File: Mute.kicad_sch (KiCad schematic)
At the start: 15 parts, among them Q1 AO3400A, SW7 SW_Push, U8 74LVC1G17, U9 SN74LVC2G74

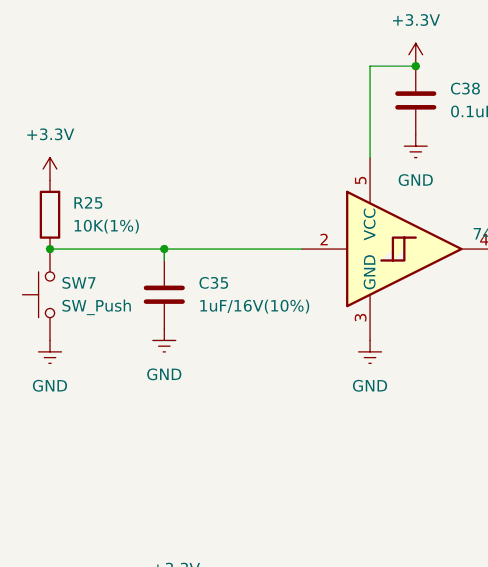
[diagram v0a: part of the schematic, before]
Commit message: Initial population of PCB
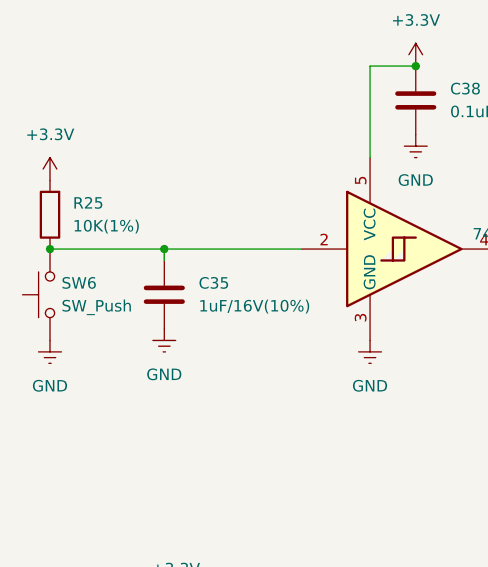
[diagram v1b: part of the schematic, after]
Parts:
- removed SW7: SW_Push, symbol Switch:SW_Push
- added SW6: SW_Push, Button_Switch_SMD:SW_SPST_PTS645, symbol Switch:SW_Push
- U8: footprint (none) -> Package_TO_SOT_SMD:SOT-23-5
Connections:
- net GND: now also SW6.1
- net at C35.1, R25.1, U8.2: now also SW6.2
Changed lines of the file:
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@@
-	)
-	(symbol
-		(lib_id "Switch:SW_Push")
-		(at 40.64 68.58 90)
-		(unit 1)
-		(exclude_from_sim no)
-		(in_bom yes)
-		(on_board yes)
-		(dnp no)
-		(fields_autoplaced yes)
-		(property "Reference" "SW7"
-			(at 41.91 67.3099 90)
-			(effects
-				(font
-					(size 1.27 1.27)
-				)
-				(justify right)
-			)
-		)
-		(property "Value" "SW_Push"
-			(at 41.91 69.8499 90)
-			(effects
-				(font
-					(size 1.27 1.27)
-				)
-				(justify right)
-			)
-		)
-		(property "Footprint" ""
-			(at 35.56 68.58 0)
-			(effects
-				(font
-					(size 1.27 1.27)
-				)
-				(hide yes)
-			)
-		)
-		(property "Datasheet" "~"
-			(at 35.56 68.58 0)
-			(effects
-				(font
-					(size 1.27 1.27)
-				)
-				(hide yes)
-			)
-		)
-		(property "Description" "Push button switch, generic, two pins"
-			(at 40.64 68.58 0)
-			(effects
-				(font
-					(size 1.27 1.27)
-				)
-				(hide yes)
-			)
-		)
-		(pin "2"
-		)
-		(pin "1"
-		)
-		(instances
-			(project "Wave"
-				(path "/d9ae5ab6-a812-4d0b-96e5-05f704754669/797be30f-7ee7-478f-9b58-a053d36acba1"
-					(reference "SW7")
-					(unit 1)
-				)
-			)
-		)
 	)
 	(symbol
@@
 			)
 		)
-		(property "Footprint" ""
+		(property "Footprint" "Package_TO_SOT_SMD:SOT-23-5"
 			(at 78.74 63.5 0)
 			(effects
@@
 					(unit 1)
 				)
+			)
+		)
+	)
+	(symbol
+		(lib_id "Switch:SW_Push")
+		(at 40.64 68.58 90)
+		(unit 1)
+		(exclude_from_sim no)
+		(in_bom yes)
+		(on_board yes)
+		(dnp no)
+		(fields_autoplaced yes)
+		(property "Reference" "SW6"
+			(at 41.91 67.3099 90)
+			(effects
+				(font
+					(size 1.27 1.27)
+				)
+				(justify right)
+			)
+		)
+		(property "Value" "SW_Push"
+			(at 41.91 69.8499 90)
+			(effects
+				(font
+					(size 1.27 1.27)
+				)
+				(justify right)
+			)
+		)
+		(property "Footprint" "Button_Switch_SMD:SW_SPST_PTS645"
+			(at 35.56 68.58 0)
+			(effects
+				(font
+					(size 1.27 1.27)
+				)
+				(hide yes)
+			)
+		)
+		(property "Datasheet" "~"
+			(at 35.56 68.58 0)
+			(effects
+				(font
+					(size 1.27 1.27)
+				)
+				(hide yes)
+			)
+		)
+		(property "Description" "Push button switch, generic, two pins"
+			(at 40.64 68.58 0)
+			(effects
+				(font
+					(size 1.27 1.27)
+				)
+				(hide yes)
+			)
+		)
+		(pin "2"
+		)
+		(pin "1"
+		)
+		(instances
+			(project "Wave"
+				(path "/d9ae5ab6-a812-4d0b-96e5-05f704754669/797be30f-7ee7-478f-9b58-a053d36acba1"
+					(reference "SW6")
+					(unit 1)
+				)

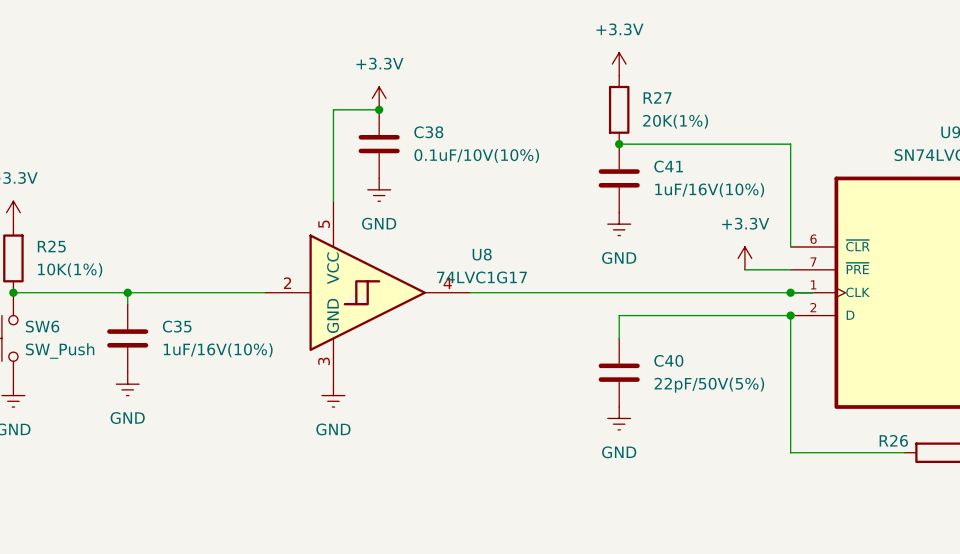
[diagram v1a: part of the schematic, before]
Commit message: Added DSP, Neopixles, MIC's and mounting holes
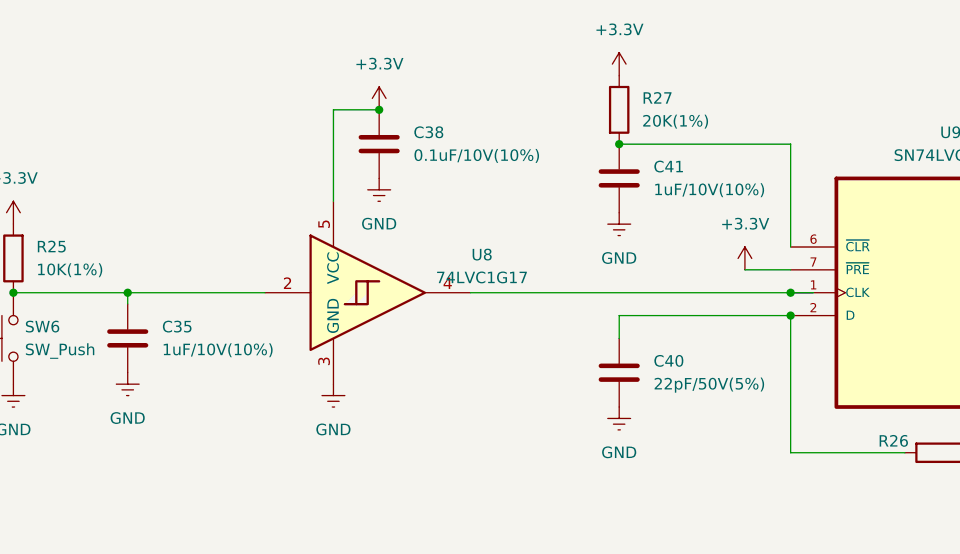
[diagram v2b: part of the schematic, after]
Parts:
- C35, C41: value 1uF/16V(10%) -> 1uF/10V(10%); footprint Capacitor_SMD:C_0603_1608Metric -> Capacitor_SMD:C_0402_1005Metric
- C38, C39, C40: footprint Capacitor_SMD:C_0603_1608Metric -> Capacitor_SMD:C_0402_1005Metric
- R25, R26, R27, R28, R29: footprint Resistor_SMD:R_0603_1608Metric -> Resistor_SMD:R_0402_1005Metric
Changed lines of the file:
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@@
 			)
 		)
-		(property "Footprint" "Resistor_SMD:R_0603_1608Metric"
+		(property "Footprint" "Resistor_SMD:R_0402_1005Metric"
 			(at 106.172 43.18 90)
 			(effects
@@
 			)
 		)
-		(property "Footprint" "Capacitor_SMD:C_0603_1608Metric"
+		(property "Footprint" "Capacitor_SMD:C_0402_1005Metric"
 			(at 82.2452 50.8 0)
 			(effects
@@
 			)
 		)
-		(property "Footprint" "Resistor_SMD:R_0603_1608Metric"
+		(property "Footprint" "Resistor_SMD:R_0402_1005Metric"
 			(at 69.85 126.238 90)
 			(effects
@@
 			)
 		)
-		(property "Value" "1uF/16V(10%)"
+		(property "Value" "1uF/10V(10%)"
 			(at 57.15 69.8499 0)
 			(effects
@@
 			)
 		)
-		(property "Footprint" "Capacitor_SMD:C_0603_1608Metric"
+		(property "Footprint" "Capacitor_SMD:C_0402_1005Metric"
 			(at 54.3052 72.39 0)
 			(effects
@@
 			)
 		)
-		(property "Footprint" "Resistor_SMD:R_0603_1608Metric"
+		(property "Footprint" "Resistor_SMD:R_0402_1005Metric"
 			(at 143.51 79.502 90)
 			(effects
@@
 			)
 		)
-		(property "Footprint" "Resistor_SMD:R_0603_1608Metric"
+		(property "Footprint" "Resistor_SMD:R_0402_1005Metric"
 			(at 42.418 59.69 90)
 			(effects
@@
 			)
 		)
-		(property "Value" "1uF/16V(10%)"
+		(property "Value" "1uF/10V(10%)"
 			(at 111.76 52.0699 0)
 			(effects
@@
 			)
 		)
-		(property "Footprint" "Capacitor_SMD:C_0603_1608Metric"
+		(property "Footprint" "Capacitor_SMD:C_0402_1005Metric"
 			(at 108.9152 54.61 0)
 			(effects
@@
 			)
 		)
-		(property "Footprint" "Capacitor_SMD:C_0603_1608Metric"
+		(property "Footprint" "Capacitor_SMD:C_0402_1005Metric"
 			(at 185.1152 60.96 0)
 			(effects
@@
 			)
 		)
-		(property "Footprint" "Resistor_SMD:R_0603_1608Metric"
+		(property "Footprint" "Resistor_SMD:R_0402_1005Metric"
 			(at 52.832 107.95 90)
 			(effects
@@
 			)
 		)
-		(property "Footprint" "Capacitor_SMD:C_0603_1608Metric"
+		(property "Footprint" "Capacitor_SMD:C_0402_1005Metric"
 			(at 108.9152 76.2 0)
 			(effects
